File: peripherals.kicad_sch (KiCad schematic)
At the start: 2 parts, among them Q4 2N7002KT1G

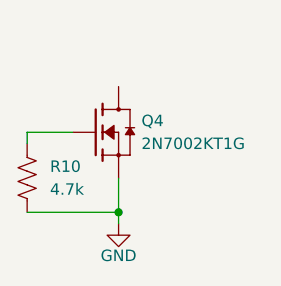
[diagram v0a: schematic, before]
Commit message: Finished gauge power circuit
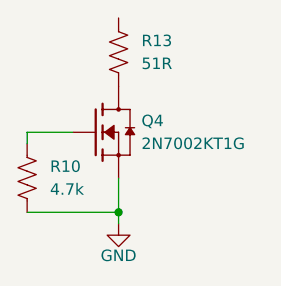
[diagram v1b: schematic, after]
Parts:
- added R13: 51R, Sullivan-Labs:R_0805_2012Metric, symbol Sullivan-Labs:RES_51R_0805
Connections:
- net at Q4.3 (D): now also R13.2
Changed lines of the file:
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@@
+	)
+	(symbol
+		(lib_id "Sullivan-Labs:RES_51R_0805")
+		(at 54.61 53.34 0)
+		(unit 1)
+		(exclude_from_sim no)
+		(in_bom yes)
+		(on_board yes)
+		(dnp no)
+		(fields_autoplaced yes)
+		(property "Reference" "R13"
+			(at 57.15 52.0699 0)
+			(effects
+				(font
+					(size 1.27 1.27)
+				)
+				(justify left)
+			)
+		)
+		(property "Value" "51R"
+			(at 57.15 54.6099 0)
+			(effects
+				(font
+					(size 1.27 1.27)
+				)
+				(justify left)
+			)
+		)
+		(property "Footprint" "Sullivan-Labs:R_0805_2012Metric"
+			(at 55.626 53.594 90)
+			(effects
+				(font
+					(size 1.27 1.27)
+				)
+				(hide yes)
+			)
+		)
+		(property "Datasheet" "~"
+			(at 54.61 53.34 0)
+			(effects
+				(font
+					(size 1.27 1.27)
+				)
+				(hide yes)
+			)
+		)
+		(property "Description" "51Ohm 0805 Resistor .5%"
+			(at 54.61 53.34 0)
+			(effects
+				(font
+					(size 1.27 1.27)
+				)
+				(hide yes)
+			)
+		)
+		(property "Manufacturer" "Panasonic"
+			(at 54.61 53.34 0)
+			(effects
+				(font
+					(size 1.27 1.27)
+				)
+				(hide yes)
+			)
+		)
+		(property "PN" "ERJ-UP6D51R0V "
+			(at 54.61 53.34 0)
+			(effects
+				(font
+					(size 1.27 1.27)
+				)
+				(hide yes)
+			)
+		)
+		(pin "2"
+		)
+		(pin "1"
+		)
+		(instances
+			(project ""
+				(path "/d013d610-c58f-4b11-9d18-37fc135ac516/216059c5-2bf9-45d1-b747-ef37194b3a11"
+					(reference "R13")
+					(unit 1)
+				)
+			)
+		)
 	)
 	(symbol

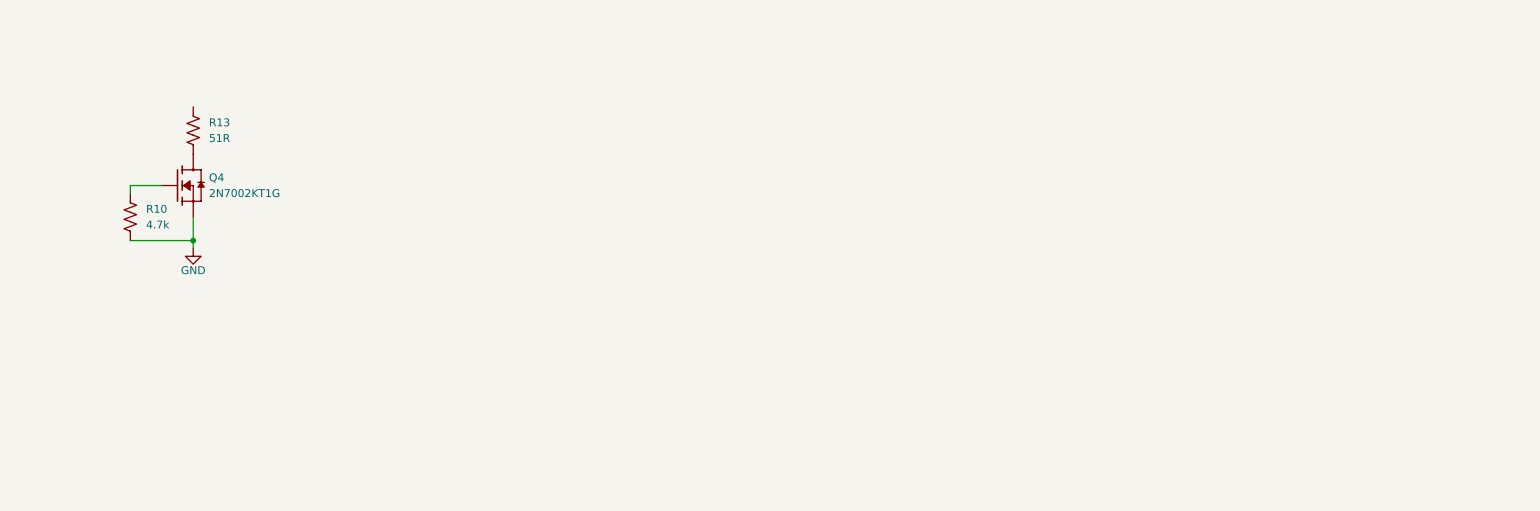
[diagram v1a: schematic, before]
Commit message: Added opto-isolated input switches and some sensor stuff
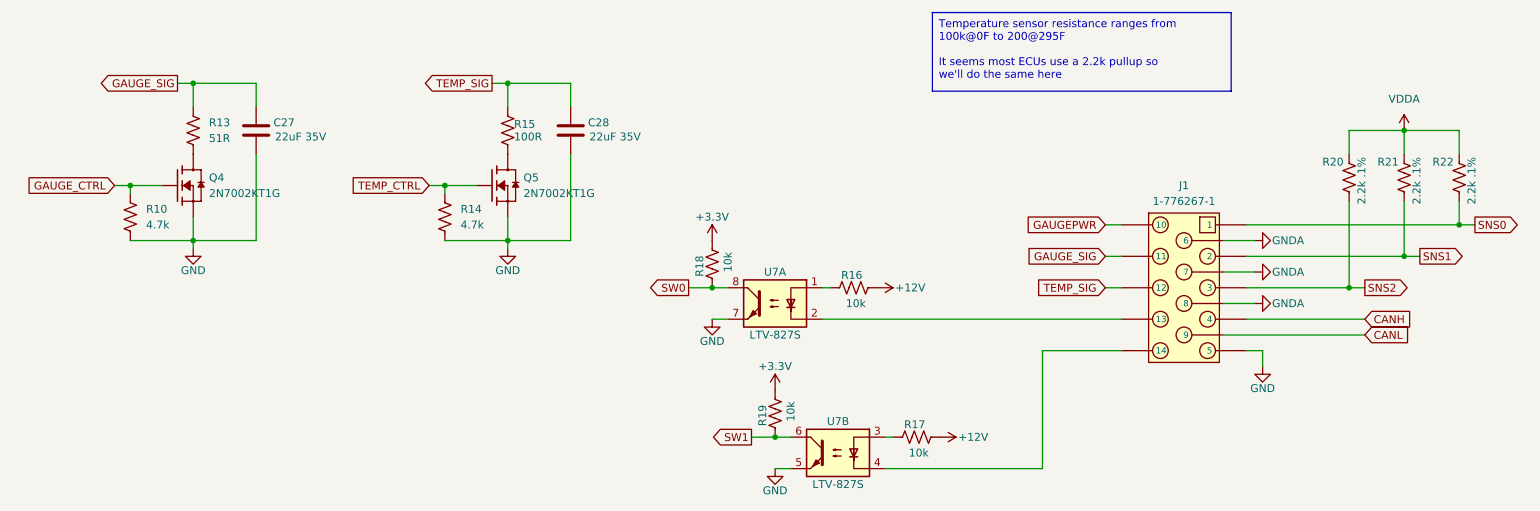
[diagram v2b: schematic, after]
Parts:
- added C27, C28: 22uF 35V, Sullivan-Labs:C_0805_2012Metric, symbol Sullivan-Labs:CAP_22uF_35V_0805
- added J1: 1-776267-1, Sullivan-Labs:TE_1-776267-1, symbol Sullivan-Labs:CONN 14-Pin AMPSEAL RA
- added Q5: 2N7002KT1G, Sullivan-Labs:SOT95P230X110-3N, symbol Sullivan-Labs:NMOS 320mA 60V
- added R14: 4.7k, Sullivan-Labs:R_0402_1005Metric, symbol Sullivan-Labs:RES_4.7k_0402
- added R15: 100R, Sullivan-Labs:R_0805_2012Metric, symbol Sullivan-Labs:RES_100R_0805
- added R16, R17, R18, R19: 10k, Sullivan-Labs:R_0402_1005Metric, symbol Sullivan-Labs:RES_10k_0402
- added R20, R21, R22: 2.2k .1%, Sullivan-Labs:R_0402_1005Metric, symbol Sullivan-Labs:RES_2.2k_.1%_0402
- added U7: LTV-827S, Sullivan-Labs:SMDIP-8_W9.53mm, symbol Sullivan-Labs:IC Opto-Isolator LTV-827S
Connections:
- net GND: now also C27.2, C28.2, J1.5, Q5.2 (S), R14.2, U7.5, U7.7
- net GAUGE_CTRL: now reaches Q4.1 (G), R10.1
- net GAUGE_SIG: now reaches R13.1
- net GAUGE_SIG: now also C27.1, J1.11
- new net: Q5.3 (D), R15.2
- new net: J1.13, U7.2
- new net: J1.14, U7.4
- new net: R16.2, U7.1
- new net: R17.2, U7.3
- new net +12V: R16.1, R17.1
- new net +3.3V: R18.1, R19.1
- new net CANH: J1.4
- new net CANL: J1.9
- new net GAUGEPWR: J1.10
- new net GNDA: J1.6, J1.7, J1.8
- new net SNS0: J1.1, R22.2
- new net SNS1: J1.2, R21.2
- new net SNS2: J1.3, R20.2
- new net SW0: R18.2, U7.8
- new net SW1: R19.2, U7.6
- new net TEMP_CTRL: Q5.1 (G), R14.1
- new net TEMP_SIG: C28.1, J1.12, R15.1
- new net VDDA: R20.1, R21.1, R22.1

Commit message: Some perpipheral changes?
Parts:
- removed J1: 1-776267-1, Sullivan-Labs:TE_1-776267-1, symbol Sullivan-Labs:CONN 14-Pin AMPSEAL RA
- added J1: 1-770669-1, Sullivan-Labs:17706691, symbol Sullivan-Labs:CONN 23-Pin AMPSEAL RA
- added R23: 2.2k .1%, Sullivan-Labs:R_0402_1005Metric, symbol Sullivan-Labs:RES_2.2k_.1%_0402
- added R24, R25, R26, R27: 10k, Sullivan-Labs:R_0402_1005Metric, symbol Sullivan-Labs:RES_10k_0402
- added U8: MCP6004T-E/ST, Sullivan-Labs:SOP65P640X120-14N, symbol Sullivan-Labs:IC 4-CH Op Amp MCP6004
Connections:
- net CANH: now also J1.15
- net CANL: now also J1.8
- net GAUGEPWR: now also J1.16
- net GAUGE_SIG: now also J1.17
- net GND: now also J1.18, J1.20
- net GNDA: now also J1.10, J1.11, J1.12, J1.9
- net TEMP_SIG: now also J1.19
- net VDDA: now also R23.1
- net at U7.2: now also J1.22
- net at U7.4: now also J1.23
- net SNS0: no longer names the net of R22.2
- net SNS0: now also J1.1, R24.1
- net SNS1: no longer names the net of R21.2
- net SNS1: now also J1.2, R25.1
- net SNS2: no longer names the net of R20.2
- net SNS2: now also J1.3, R26.1
- new net: J1.4, R23.2, R27.1
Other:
- moved on the sheet: C27, C28, Q4, Q5, R10, R13, R14, R15, R16, R17, R18, R19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

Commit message: Small changes to schematic
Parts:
- added C38, C39: .1uF 25V, Sullivan-Labs:C_0402_1005Metric, symbol Sullivan-Labs:CAP_.1uF_25V_0402
- added J2: 12AWG Wire Pads, Sullivan-Labs:6-pin 12AWG Wire Pads, symbol Sullivan-Labs:CONN_6P_12GA_WIREPADS
- added R28, R30, R32, R34: 5.6k .1%, Sullivan-Labs:R_0402_1005Metric, symbol Sullivan-Labs:RES_5.6k_.1%_0402
- added R29, R31, R33, R35: 10k .1%, Sullivan-Labs:R_0402_1005Metric, symbol Sullivan-Labs:RES_10k_.1%_0402
- added R40: 120R, Sullivan-Labs:R_0603_1608Metric, symbol Sullivan-Labs:RES_120R_0603
- added U3: MCP2542FD, Sullivan-Labs:SOIC8_4P9X3P9MC_MCH, symbol Sullivan-Labs:IC MCP2542FD CAN Transceiver
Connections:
- net VDDA is gone; now on net +5V: R20.1, R21.1, R22.1, R23.1
- net +3.3V: now also C39.1, U3.5 (VIO)
- net AUX: now also R34.1, R35.1
- net GND: now also C38.2, C39.2, U3.2 (VSS)
- net GNDA: now also U8.11 (V-), R29.2, R31.2, R33.2, R35.2
- net OIL: now also R30.1, R31.1
- net TRANS: now also R32.1, R33.1
- net WATER: now also R28.1, R29.1
- net at U8.1: now also U8.2 (-), R28.2
- net at U8.3 (+): now also R24.2
- net at U8.12 (+): now also R27.2
- net at U8.13 (-): now also U8.14, R34.2
- net at R25.2: now also U8.5 (+)
- net at U8.6 (-): now also U8.7, R30.2
- net at U8.10 (+): now also R26.2
- net at U8.8: now also U8.9 (-), R32.2
- net +5V: now reaches U8.4 (V+)
- net +5V: now also C38.1, U3.3 (VDD)
- net CANH renamed CAN_P
- net CAN_P: now also R40.1, U3.7 (CANH)
- net CANL renamed CAN_N
- net CAN_N: now also R40.2, U3.6 (CANL)
- new net CAN_RX: U3.4 (RXD)
- new net CAN_TX: U3.1 (TXD)
- new net OUT0: J2.1
- new net OUT1: J2.2
- new net OUT2: J2.3
- new net OUT3: J2.4
- new net OUT4: J2.5
- new net OUT5: J2.6
- new net STBY: U3.8 (STBY)
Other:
- moved on the sheet: U8A, U8B, U8C, U8D, U8E

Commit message: Initial schematic is done
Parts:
- removed J2: 12AWG Wire Pads, Sullivan-Labs:6-pin 12AWG Wire Pads, symbol Sullivan-Labs:CONN_6P_12GA_WIREPADS
- added C52, C53, C54, C55: 1nF 25V, Sullivan-Labs:C_0402_1005Metric, symbol Sullivan-Labs:CAP_1nF_25V_0402
- added D13: ESDA25-4BP6, Sullivan-Labs:SOT666_ESDA25_STM, symbol Sullivan-Labs:DIODE 4CH 24Vwm 50W
- added D14, D15, D6, D7, D8, D9: 5V, Sullivan-Labs:ESD9B5.0ST5G, symbol Sullivan-Labs:DIODE TVS 5Vwm
- added J2: 19437-0029, Sullivan-Labs:MOLEX_19437-0029, symbol Sullivan-Labs:CONN 4-Pin 40A Molex
- added J4: M6 Stud, Sullivan-Labs:WP-BUCF_7461059, symbol Sullivan-Labs:TERM M6 240A
- added R44, R45, R46, R47: 10k, Sullivan-Labs:R_0402_1005Metric, symbol Sullivan-Labs:RES_10k_0402
- added R48, R49, R50, R51: 100R, Sullivan-Labs:R_0402_1005Metric, symbol Sullivan-Labs:RES_100R_0402
- added U9: LTV-827S, Sullivan-Labs:SMDIP-8_W9.53mm, symbol Sullivan-Labs:IC Opto-Isolator LTV-827S
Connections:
- net +3.3V: now also R44.1, R45.1
- net CAN_N: now also J1.14, D15.2; no longer J1.8
- net CAN_P: now also J1.6, D14.2; no longer J1.15
- net GND: now also J1.13, J1.5, U7.2, U7.4, C52.2, C53.2, C54.2, C55.2, D13.2, D13.5, D14.1, D15.1, D6.2, D7.2, D8.2, D9.2, U9.2, U9.4, U9.5, U9.7; no longer J1.20
- net OUT0: now also J2.1
- net OUT1: now also J2.2
- net OUT2: now also J2.3
- net OUT3: now also J2.4
- net SW0: now also R48.1; no longer R18.2, U7.8
- net SW1: now also R49.1; no longer R19.2, U7.6
- net at R24.2, U8.3 (+): now also C54.1, C55.1
- net at J1.1, R22.2, R24.1: now also D6.1
- net at R27.2, U8.12 (+): now also C52.1
- net at J1.4, R23.2, R27.1: now also D9.1
- net at J1.2, R21.2, R25.1: now also D7.1
- net at J1.3, R20.2, R26.1: now also D8.1
- net at R26.2, U8.10 (+): now also C53.1
- net IN1: now reaches J1.21
- net IN1: now also R17.1, D13.3
- net IN2: now reaches J1.22
- net IN2: now also D13.6, R46.1; no longer U7.2
- net IN3: now reaches J1.23
- net IN3: now also D13.4, R47.1; no longer U7.4
- net IGN: now reaches J1.7
- net +12V renamed IN0
- net IN0: now also J1.20, D13.1; no longer R17.1
- net AUX renamed SNS3
- net OIL renamed SNS1
- net TRANS renamed SNS2
- net WATER renamed SNS0
- new net: R18.2, R48.2, U7.8
- new net: R44.2, R50.2, U9.8
- new net: R46.2, U9.1
- new net: R45.2, R51.2, U9.6
- new net: R19.2, R49.2, U7.6
- new net: R47.2, U9.3
- new net LP_OUT0: J1.15
- new net LP_OUT1: J1.8
- new net SW2: R50.1
- new net SW3: R51.1
- new net VDC: J4.1
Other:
- moved on the sheet: J1, R16, R17, R18, R19, R20, R21, R22, R23, R24, R25, R26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
